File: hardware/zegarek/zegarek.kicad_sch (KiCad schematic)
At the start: 14 parts, among them SW2 SW_Push, SW3 SW_Push, SW4 SW_Push

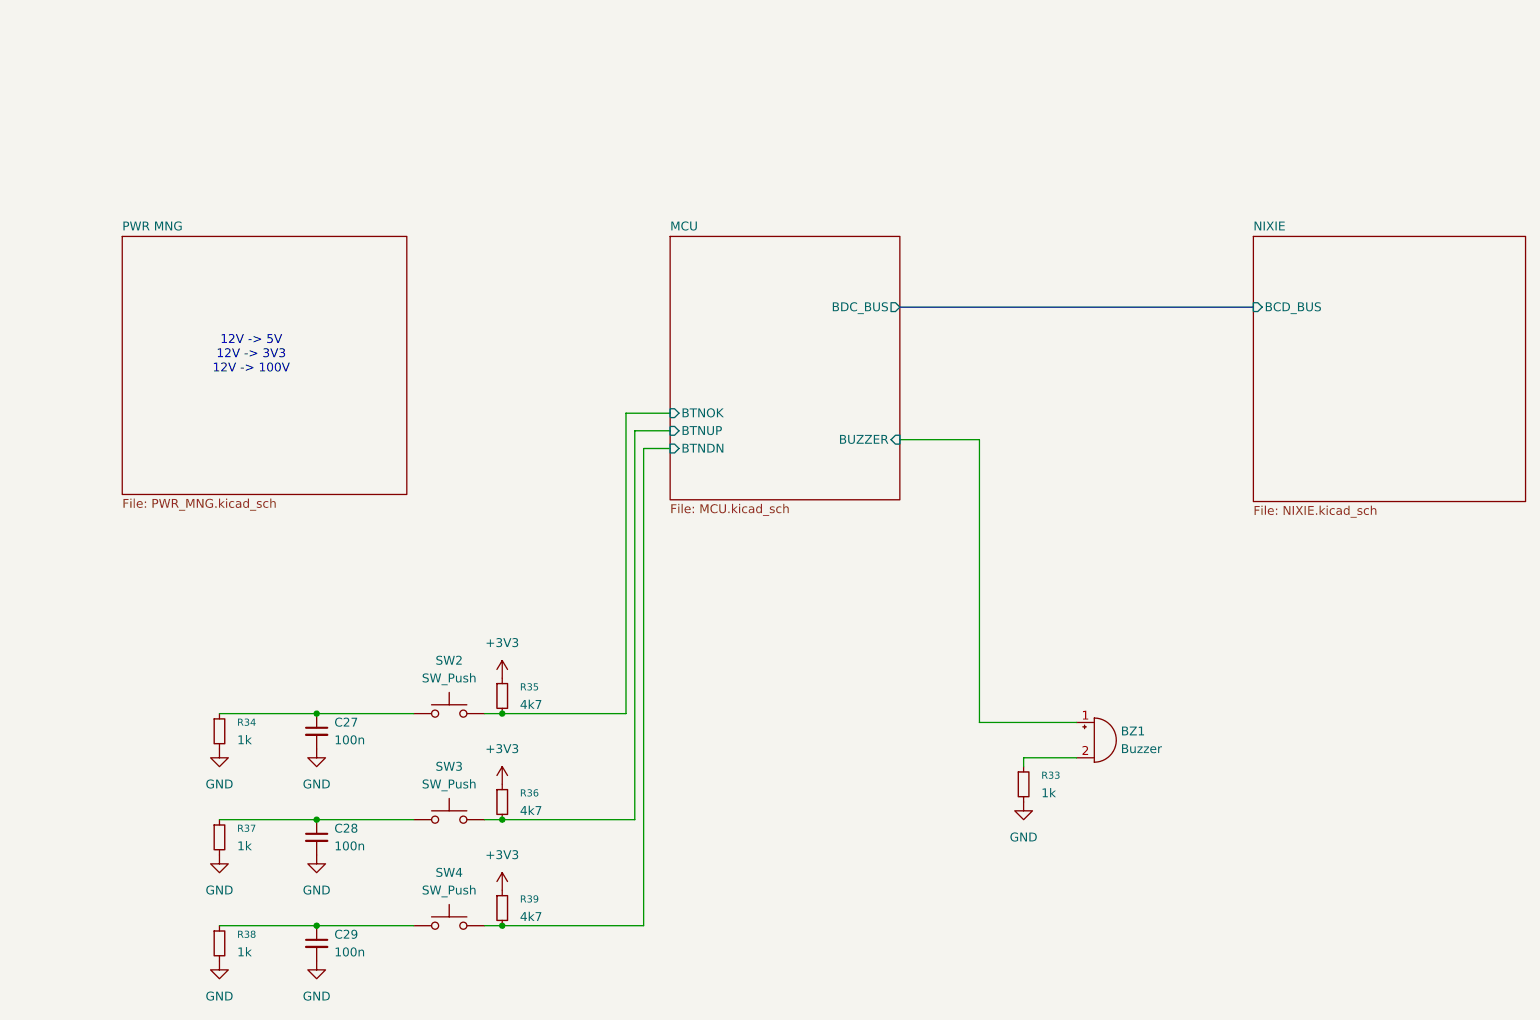
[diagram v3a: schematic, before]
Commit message: done placing footprins on pcb, started tracing pcb
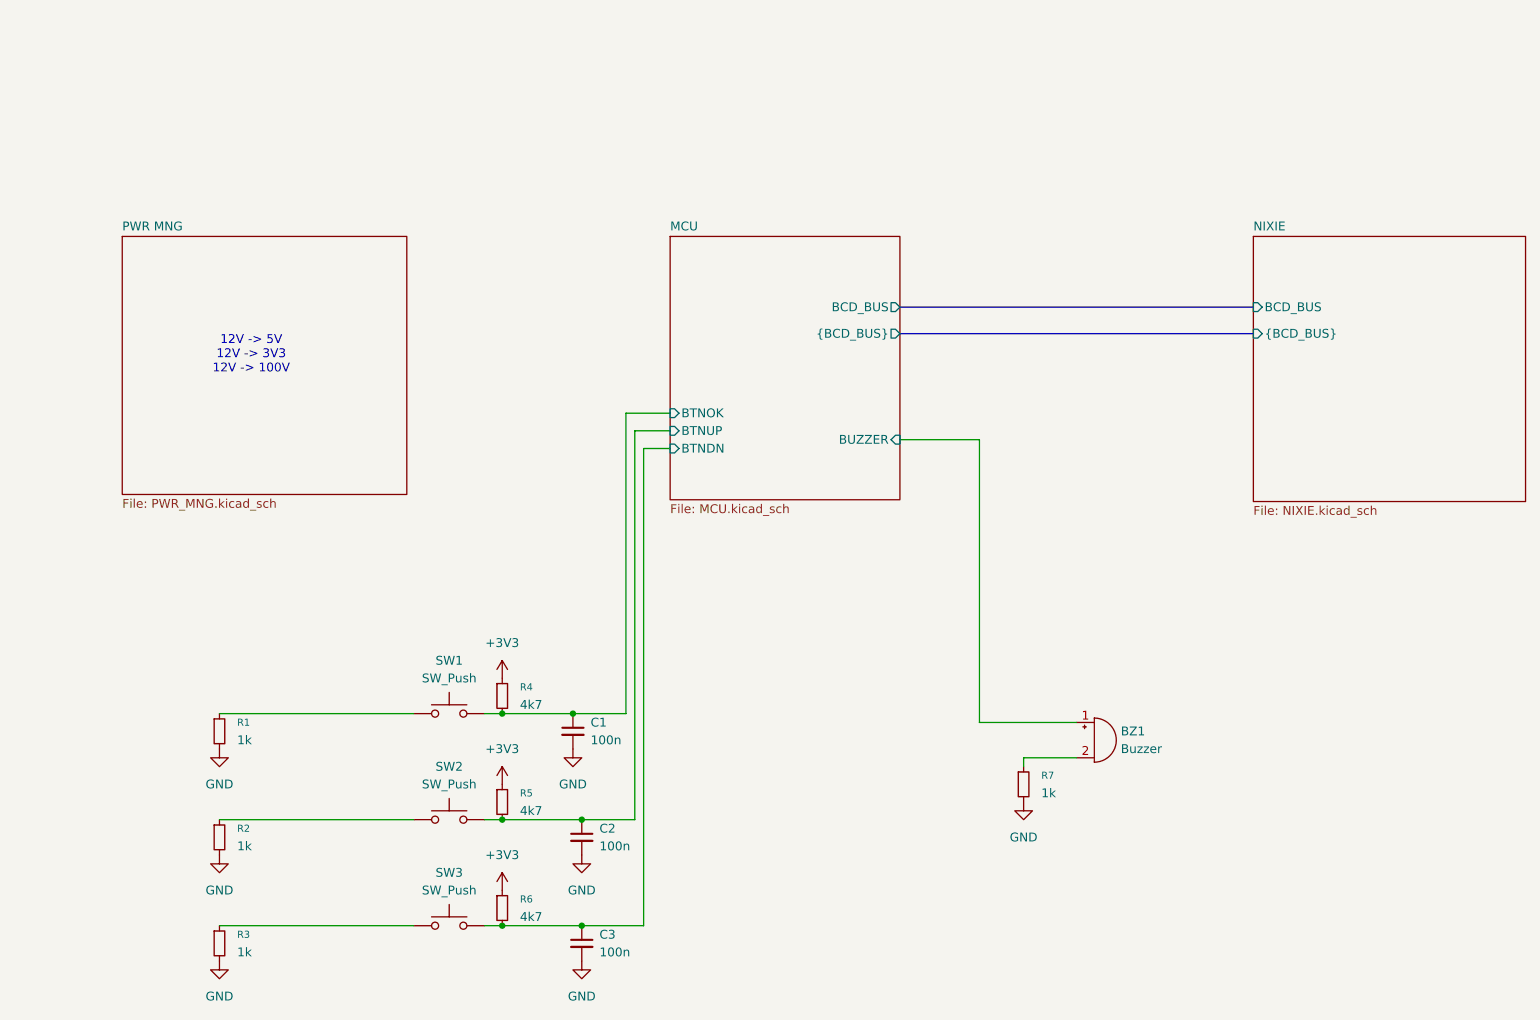
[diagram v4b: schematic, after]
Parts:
- R1: renamed from R34; footprint Resistor_SMD:R_0201_0603Metric_Pad0.64x0.40mm_HandSolder -> Resistor_SMD:R_0603_1608Metric_Pad0.98x0.95mm_HandSolder
- R3: renamed from R38; footprint Resistor_SMD:R_0201_0603Metric_Pad0.64x0.40mm_HandSolder -> Resistor_SMD:R_0603_1608Metric_Pad0.98x0.95mm_HandSolder
- R4: renamed from R35; footprint Resistor_SMD:R_0201_0603Metric_Pad0.64x0.40mm_HandSolder -> Resistor_SMD:R_0603_1608Metric_Pad0.98x0.95mm_HandSolder
- R5: renamed from R36; footprint Resistor_SMD:R_0201_0603Metric_Pad0.64x0.40mm_HandSolder -> Resistor_SMD:R_0603_1608Metric_Pad0.98x0.95mm_HandSolder
- R6: renamed from R39; footprint Resistor_SMD:R_0201_0603Metric_Pad0.64x0.40mm_HandSolder -> Resistor_SMD:R_0603_1608Metric_Pad0.98x0.95mm_HandSolder
- R7: renamed from R33; footprint Resistor_SMD:R_0201_0603Metric_Pad0.64x0.40mm_HandSolder -> Resistor_SMD:R_0603_1608Metric_Pad0.98x0.95mm_HandSolder
- renumbered C27 to C1, C28 to C2, C29 to C3, R37 to R2, SW2 to SW1, SW3 to SW2, SW4 to SW3
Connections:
- net MCU/BTNDN: now also C3.1
- net MCU/BTNOK: now also C1.1
- net MCU/BTNUP: now also C2.1
- net at R2.1, SW2.1: no longer C2.1
- net at R1.1, SW1.1: no longer C1.1
- net at R3.1, SW3.1: no longer C3.1
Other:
- sheet MCU ports: added BCD_BUS, {BCD_BUS}; removed BDC_BUS
- sheet NIXIE ports: added {BCD_BUS}; removed none
- moved on the sheet: C1, C2, C3

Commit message: pwr tracing done
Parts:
- R2: footprint Resistor_SMD:R_0201_0603Metric_Pad0.64x0.40mm_HandSolder -> Resistor_SMD:R_0603_1608Metric_Pad0.98x0.95mm_HandSolder
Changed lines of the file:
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@@
 			)
 		)
-		(property "Footprint" "Resistor_SMD:R_0201_0603Metric_Pad0.64x0.40mm_HandSolder"
+		(property "Footprint" "Resistor_SMD:R_0603_1608Metric_Pad0.98x0.95mm_HandSolder"
 			(at 54.61 137.16 0)
 			(hide yes)

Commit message: jlc generated bom and grb+drill
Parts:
- C1, C2, C3: LCSC (none) -> C152824
- R1, R3, R7: LCSC (none) -> C2074140
- R4, R5, R6: LCSC (none) -> C3152147
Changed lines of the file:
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@@
+			)
+		)
+		(property "LCSC" "C152824"
+			(at 109.22 135.8962 0)
+			(effects
+				(font
+					(size 1.27 1.27)
+				)
+				(hide yes)
 			)
 		)
@@
 			)
 		)
+		(property "LCSC" "C3152147"
+			(at 97.79 146.0499 0)
+			(effects
+				(font
+					(size 1.27 1.27)
+				)
+				(hide yes)
+			)
+		)
 		(pin "1"
 		)
@@
 			)
 		)
+		(property "LCSC" "C2074140"
+			(at 57.15 120.6499 0)
+			(effects
+				(font
+					(size 1.27 1.27)
+				)
+				(hide yes)
+			)
+		)
 		(pin "1"
 		)
@@
 			)
 		)
+		(property "LCSC" "C3152147"
+			(at 97.79 115.5699 0)
+			(effects
+				(font
+					(size 1.27 1.27)
+				)
+				(hide yes)
+			)
+		)
 		(pin "1"
 		)
@@
 			)
 		)
+		(property "LCSC" "C2074140"
+			(at 57.15 151.1299 0)
+			(effects
+				(font
+					(size 1.27 1.27)
+				)
+				(hide yes)
+			)
+		)
 		(pin "1"
 		)
@@
 			)
 		)
+		(property "LCSC" "C2074140"
+			(at 172.72 128.2699 0)
+			(effects
+				(font
+					(size 1.27 1.27)
+				)
+				(hide yes)
+			)
+		)
 		(pin "1"
 		)
@@
 			)
 		)
+		(property "LCSC" "C152824"
+			(at 107.95 120.6562 0)
+			(effects
+				(font
+					(size 1.27 1.27)
+				)
+				(hide yes)
+			)
+		)
 		(pin "1"
 		)
@@
 			)
 		)
+		(property "LCSC" "C3152147"
+			(at 97.79 130.8099 0)
+			(effects
+				(font
+					(size 1.27 1.27)
+				)
+				(hide yes)
+			)
+		)
 		(pin "1"
 		)
@@
 			)
 		)
+		(property "LCSC" "C152824"
+			(at 109.22 151.1362 0)
+			(effects
+				(font
+					(size 1.27 1.27)
+				)
+				(hide yes)
+			)
+		)

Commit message: correction changes, postprod files regenration,added OE and EN to MCU schematic
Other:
- sheet MCU ports: added ~{OE}; removed none
- sheet NIXIE ports: added ~{OE}; removed none
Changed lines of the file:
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@@
+	(wire
+		(pts
+			(xy 152.4 68.58) (xy 203.2 68.58)
+		)
+		(stroke
+			(width 0)
+			(type default)
+		)
+	)
 	(wire
 		(pts
@@
 			)
 		)
+		(pin "~{OE}" input
+			(at 152.4 68.58 0)
+			(effects
+				(font
+					(size 1.27 1.27)
+				)
+				(justify right)
+			)
+		)
 		(instances
 			(project "zegarek"
@@
 			(effects
 				(font
+					(size 1.27 1.27)
+				)
+				(justify left)
+			)
+		)
+		(pin "~{OE}" input
+			(at 203.2 68.58 180)
+			(effects
+				(font
